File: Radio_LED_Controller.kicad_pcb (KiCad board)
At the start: 2 copper layers, 21.5 x 12.5 mm, 15 parts, among them J1 Conn_01x04_Pin, J2 Conn_01x03_Pin, J3 Conn_01x05, J4 UPDI, J5 Conn_01x02_Pin, J6 Conn_01x02_Pin, J7 Conn_01x05, Q2 SS8050, Q3 SS8050, U1 ATtiny816-M

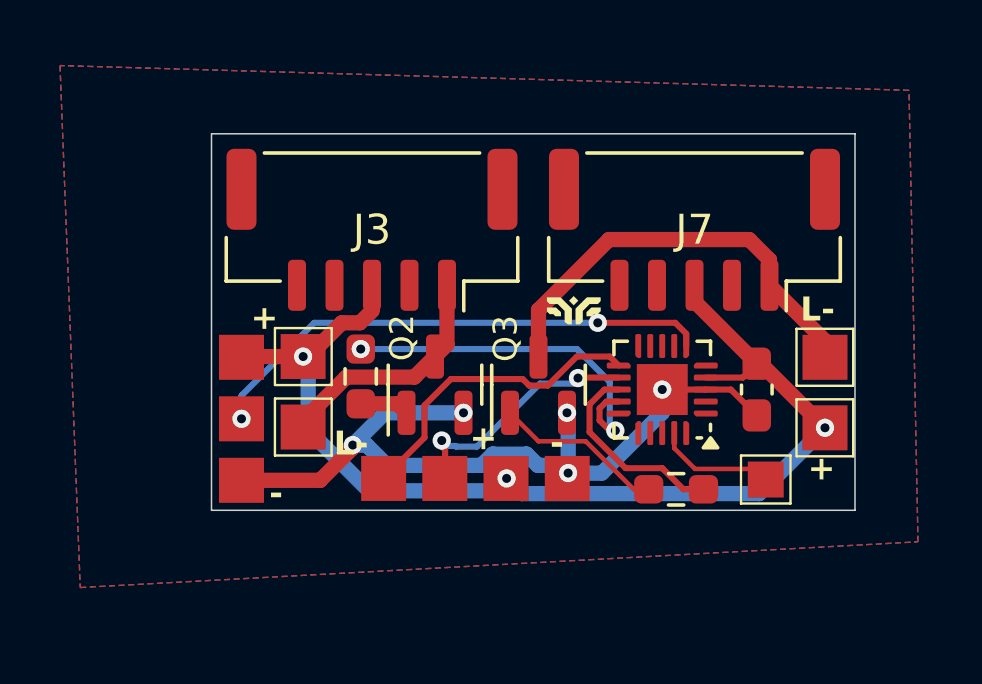
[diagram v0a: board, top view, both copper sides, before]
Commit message: extra 2 RGB port
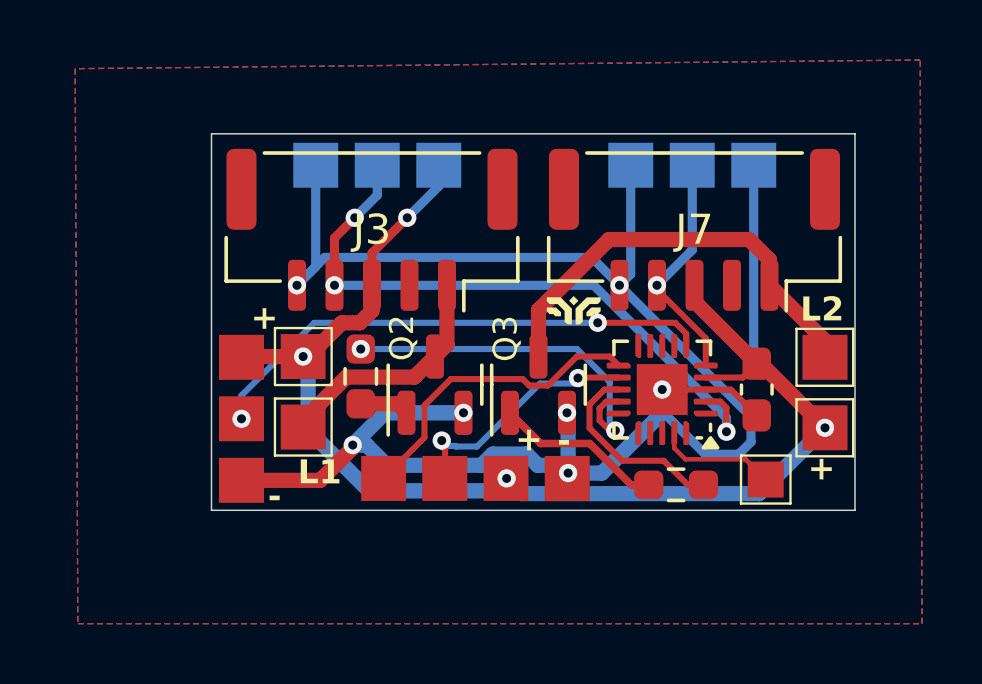
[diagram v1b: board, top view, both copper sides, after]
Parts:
- added J8: Conn_01x03_Pin, MyLib:SolderPad_01x03_1.5mm, B.Cu at (171.8, 85.5)
- added J9: Conn_01x03_Pin, MyLib:SolderPad_01x03_1.5mm, B.Cu at (182.3, 85.5)
- C2: value 1uF -> 10uF
- moved G*** 3.46 mm to (181.2, 89.5)
- moved R3 0.15 mm to (178.7, 95.2)
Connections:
- net RGB renamed RGB3
- J3 pad 4: unconnected-(J3-Pin_4-Pad4) -> RGB1
- J3 pad 5: unconnected-(J3-Pin_5-Pad5) -> GND
- J7 pad 4: unconnected-(J7-Pin_4-Pad4) -> RGB2
- J7 pad 5: unconnected-(J7-Pin_5-Pad5) -> GND
- U1 pad 2: unconnected-(U1-PA3-Pad2) -> RGB1
- U1 pad 5: unconnected-(U1-PA4-Pad5) -> RGB2
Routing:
- net GND: track 26.5 -> 58.0 mm, vias 5 -> 7
- net RGB1: track 0.00 -> 21.5 mm, vias 0 -> 3
- net VCC: track 36.2 -> 50.9 mm, vias 3 -> 4
- net RGB2: track 0.00 -> 7.83 mm, vias 0 -> 1
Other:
- board text added: "L1"
- board text added: "L2"
- board text added: "RGB1"
- board text added: "RGB2"
- board text added: "RGB3"
- board text removed: "L-"
